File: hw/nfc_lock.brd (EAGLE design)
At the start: 100 x 80 mm, 0 parts

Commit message: CPU + NFC
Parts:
- added IC1: STM8S003F3, stm8:TSSOP20
- added U1: M24SR16-YMN6T/2, m24sr16-ymn6t_2:SOIC127P600X175-8N
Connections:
- new net GND: IC1.7
- new net VCAP: IC1.8
- new net VCC: U1.8
- new net VDD: IC1.9
- new net VSS: U1.4
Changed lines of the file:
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@@
 </autorouter>
 <elements>
+<element name="U1" library="m24sr16-ymn6t_2" package="SOIC127P600X175-8N" value="M24SR16-YMN6T/2" x="20.32" y="17.78">
+<attribute name="PACKAGE" value="SO-8 STMicroelectronics" x="20.32" y="17.78" size="1.778" layer="27" display="off"/>
+<attribute name="PRICE" value="0.81 USD" x="20.32" y="17.78" size="1.778" layer="27" display="off"/>
+<attribute name="MP" value="M24SR16-YMN6T/2" x="20.32" y="17.78" size="1.778" layer="27" display="off"/>
+<attribute name="DESCRIPTION" value=" NFC/RFID Tag and Transponder Chip 13553kHz to 13567kHz 16Kbit 8-Pin SO N Tape and Reel " x="20.32" y="17.78" size="1.778" layer="27" display="off"/>
+<attribute name="AVAILABILITY" value="Good" x="20.32" y="17.78" size="1.778" layer="27" display="off"/>
+<attribute name="MF" value="STMicroelectronics" x="20.32" y="17.78" size="1.778" layer="27" display="off"/>
+</element>
+<element name="IC1" library="stm8" package="TSSOP20" value="STM8S003F3" x="31.75" y="34.29" rot="R270"/>
 </elements>
 <signals>
+<signal name="VCC">
+<contactref element="U1" pad="8"/>
+</signal>
+<signal name="VSS">
+<contactref element="U1" pad="4"/>
+</signal>
+<signal name="VDD">
+<contactref element="IC1" pad="9"/>
+</signal>
+<signal name="VCAP">
+<contactref element="IC1" pad="8"/>
+</signal>
+<signal name="GND">
+<contactref element="IC1" pad="7"/>
+</signal>
 </signals>
 </board>

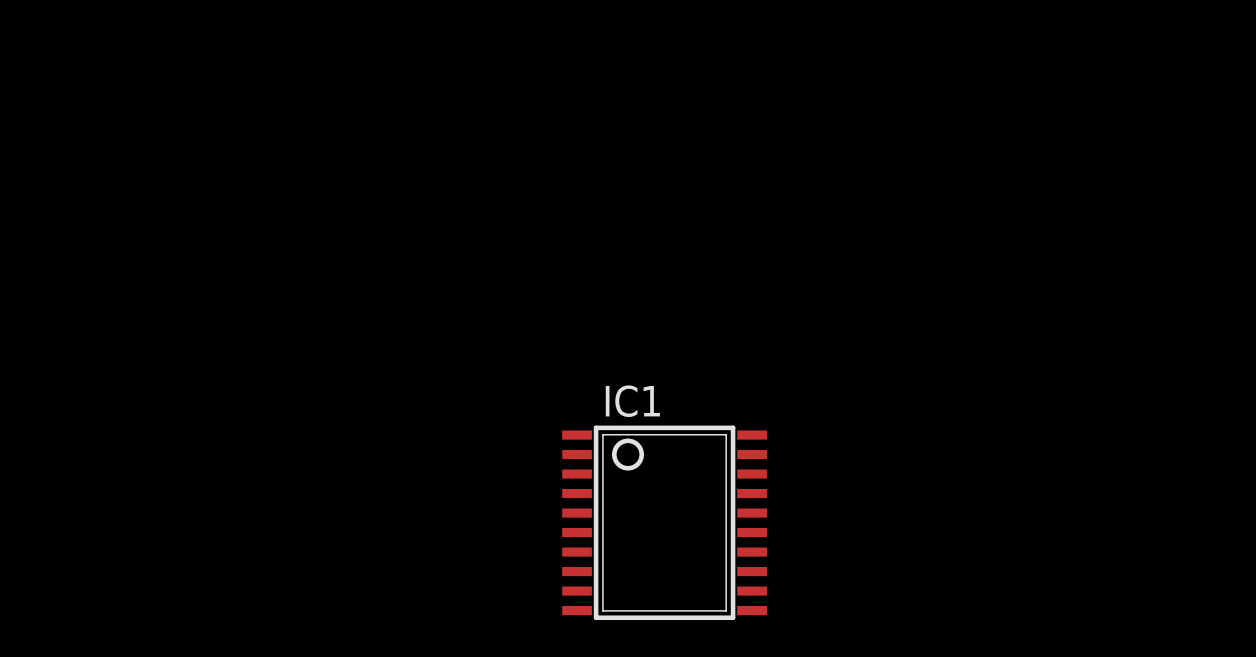
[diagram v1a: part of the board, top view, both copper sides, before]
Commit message: 3.3 voltage regulators + I2C lines
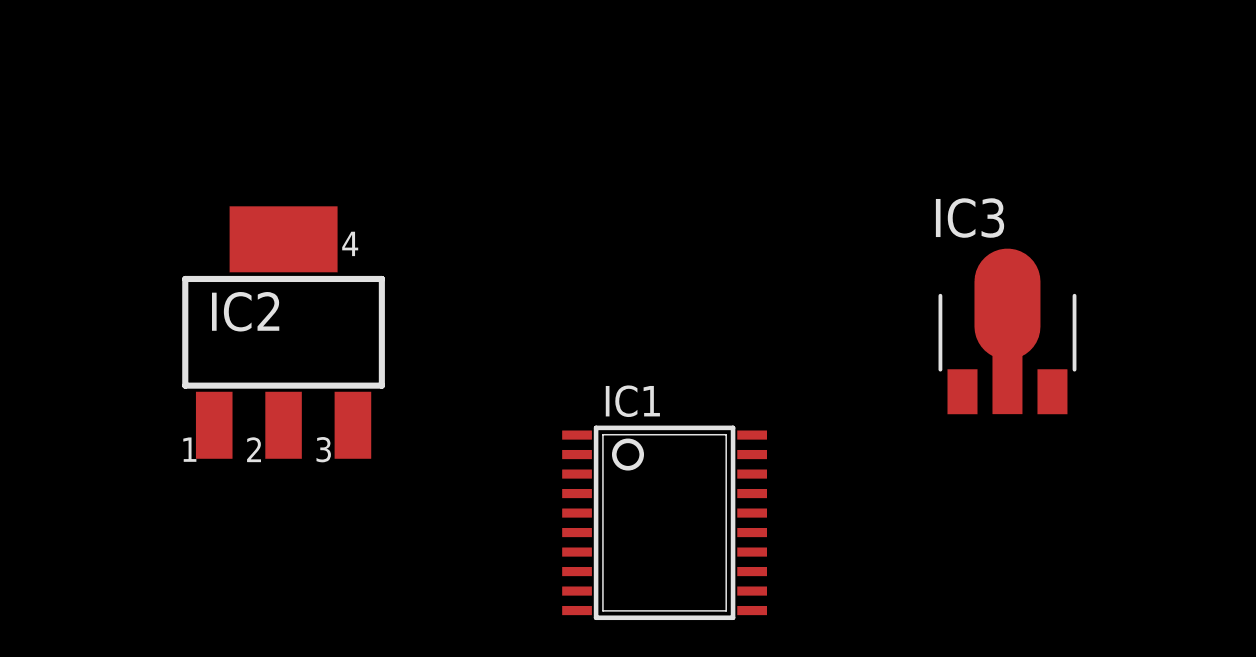
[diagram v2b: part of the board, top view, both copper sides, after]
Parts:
- added IC2: MCP1703DB, linear:SOT223
- added IC3: MCP170312MB, linear:SOT89
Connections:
- new net N$1: IC1.12, U1.6
- new net N$2: IC1.11, U1.5
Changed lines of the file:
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@@
 </element>
 <element name="IC1" library="stm8" package="TSSOP20" value="STM8S003F3" x="31.75" y="34.29" rot="R270"/>
+<element name="IC2" library="linear" package="SOT223" value="MCP1703DB" x="19.05" y="40.64"/>
+<element name="IC3" library="linear" package="SOT89" value="MCP170312MB" x="43.18" y="40.64"/>
 </elements>
 <signals>
@@
 <contactref element="IC1" pad="7"/>
 </signal>
+<signal name="N$1">
+<contactref element="IC1" pad="12"/>
+<contactref element="U1" pad="6"/>
+<wire x1="22.6822" y1="17.145" x2="34.6678" y2="32.015" width="0" layer="19" extent="1-1"/>
+</signal>
+<signal name="N$2">
+<contactref element="IC1" pad="11"/>
+<contactref element="U1" pad="5"/>
+<wire x1="22.6822" y1="15.875" x2="34.6678" y2="31.365" width="0" layer="19" extent="1-1"/>
+</signal>
 </signals>

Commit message: power supply circut
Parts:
- removed IC2: MCP1703DB, linear:SOT223
- added C2: (no value), rcl:153CLV-0405
- added C3: (no value), rcl:C1206
- added D1, D2: GF1, diode:SMA-DO214AC
- moved IC3 7.62 mm to (43.2, 48.3)
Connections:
- new net +5V: D1.A
- new net +5V/1: C3.1, IC3.3
- new net 0V: C2.-, C3.2, IC3.1
- new net N$3: D1.K, D2.A
- new net N$4: C2.+, D2.K, IC3.2@1
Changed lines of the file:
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@@
 <layer number="97" name="Info" color="7" fill="1" visible="no" active="no"/>
 <layer number="98" name="Guide" color="6" fill="1" visible="no" active="no"/>
+<layer number="99" name="SpiceOrder" color="5" fill="1" visible="no" active="no"/>
 </layers>
 <board>
@@
 </element>
 <element name="IC1" library="stm8" package="TSSOP20" value="STM8S003F3" x="31.75" y="34.29" rot="R270"/>
-<element name="IC2" library="linear" package="SOT223" value="MCP1703DB" x="19.05" y="40.64"/>
-<element name="IC3" library="linear" package="SOT89" value="MCP170312MB" x="43.18" y="40.64"/>
+<element name="IC3" library="linear" package="SOT89" value="MCP170312MB" x="43.18" y="48.26"/>
+<element name="C2" library="rcl" package="153CLV-0405" value="" x="36.83" y="48.26" rot="R90"/>
+<element name="C3" library="rcl" package="C1206" value="" x="43.18" y="41.91" rot="R180"/>
+<element name="D1" library="diode" package="SMA-DO214AC" value="GF1" x="31.75" y="54.61"/>
+<element name="D2" library="diode" package="SMA-DO214AC" value="GF1" x="41.91" y="54.61"/>
 </elements>
 <signals>
@@
 <wire x1="22.6822" y1="15.875" x2="34.6678" y2="31.365" width="0" layer="19" extent="1-1"/>
 </signal>
+<signal name="0V">
+<contactref element="IC3" pad="1"/>
+<contactref element="C3" pad="2"/>
+<contactref element="C2" pad="-"/>
+<wire x1="41.681" y1="46.279" x2="41.78" y2="41.91" width="0" layer="19" extent="1-1"/>
+<wire x1="36.83" y1="46.46" x2="41.681" y2="46.279" width="0" layer="19" extent="1-1"/>
+</signal>
+<signal name="+5V/1">
+<contactref element="IC3" pad="3"/>
+<contactref element="C3" pad="1"/>
+<wire x1="44.679" y1="46.279" x2="44.58" y2="41.91" width="0" layer="19" extent="1-1"/>
+</signal>
+<signal name="+5V">
+<contactref element="D1" pad="A"/>
+</signal>
+<signal name="N$3">
+<contactref element="D1" pad="K"/>
+<contactref element="D2" pad="A"/>
+<wire x1="39.86" y1="54.61" x2="33.8" y2="54.61" width="0" layer="19" extent="1-1"/>
+</signal>
+<signal name="N$4">
+<contactref element="IC3" pad="2@1"/>
+<contactref element="D2" pad="K"/>
+<contactref element="C2" pad="+"/>
+<wire x1="36.83" y1="50.06" x2="43.18" y2="49.2" width="0" layer="19" extent="1-1"/>
+<wire x1="43.96" y1="54.61" x2="43.18" y2="49.2" width="0" layer="19" extent="1-1"/>
+</signal>
 </signals>

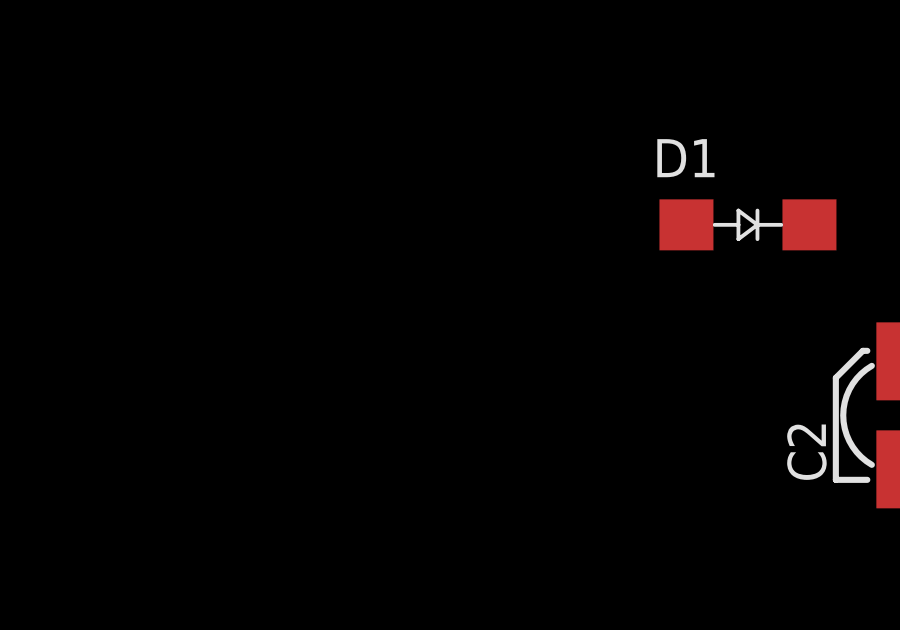
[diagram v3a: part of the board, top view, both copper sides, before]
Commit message: power supply pads added
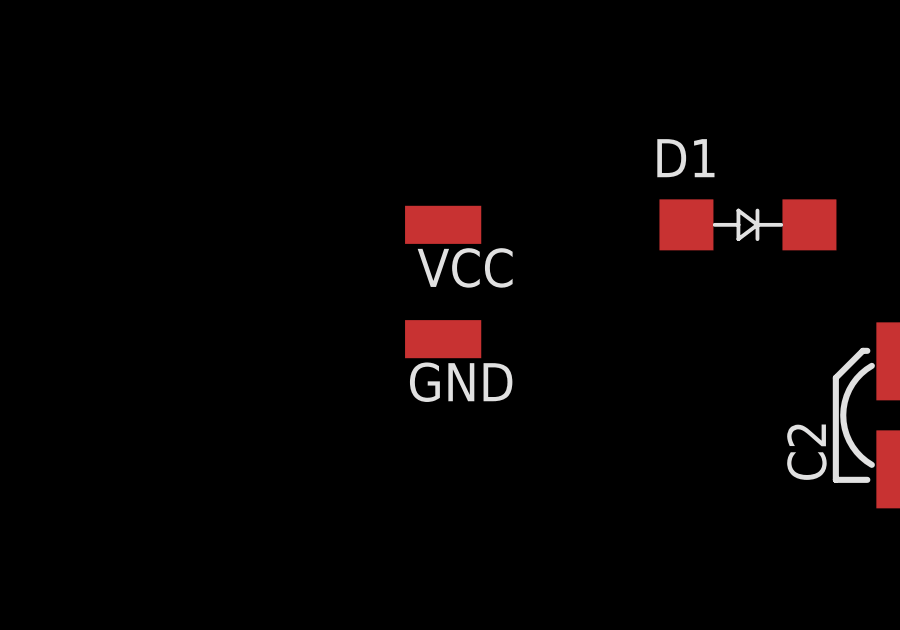
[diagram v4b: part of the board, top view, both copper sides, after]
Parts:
- added GND, VCC: (no value), wirepad:SMD1,27-2,54
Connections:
- net +5V: now also VCC.1
- net 0V: now also GND.1
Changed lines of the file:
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@@
 <element name="D1" library="diode" package="SMA-DO214AC" value="GF1" x="31.75" y="54.61"/>
 <element name="D2" library="diode" package="SMA-DO214AC" value="GF1" x="41.91" y="54.61"/>
+<element name="VCC" library="wirepad" package="SMD1,27-2,54" value="" x="21.59" y="54.61" rot="R90"/>
+<element name="GND" library="wirepad" package="SMD1,27-2,54" value="" x="21.59" y="50.8" rot="R90"/>
 </elements>
 <signals>
@@
 <contactref element="C3" pad="2"/>
 <contactref element="C2" pad="-"/>
-<wire x1="41.681" y1="46.279" x2="41.78" y2="41.91" width="0" layer="19" extent="1-1"/>
+<contactref element="GND" pad="1"/>
+<wire x1="41.78" y1="41.91" x2="41.681" y2="46.279" width="0" layer="19" extent="1-1"/>
 <wire x1="36.83" y1="46.46" x2="41.681" y2="46.279" width="0" layer="19" extent="1-1"/>
+<wire x1="21.59" y1="50.8" x2="41.78" y2="41.91" width="0" layer="19" extent="1-1"/>
 </signal>
 <signal name="+5V/1">
@@
 <signal name="+5V">
 <contactref element="D1" pad="A"/>
+<contactref element="VCC" pad="1"/>
+<wire x1="21.59" y1="54.61" x2="29.7" y2="54.61" width="0" layer="19" extent="1-1"/>
 </signal>
 <signal name="N$3">

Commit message: USB powersupply
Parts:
- removed GND, VCC: (no value), wirepad:SMD1,27-2,54
- added X1: MINI-USB-32005-301, con-cypressindustries:32005-301
- moved U1 14.5 mm to (31.8, 26.7)
- moved D1 2.54 mm to (31.8, 52.1), turned to 90 degrees
- moved IC1 1.27 mm to (31.8, 35.6)
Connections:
- removed net GND: IC1.7
- removed net VCC: U1.8
- removed net VDD: IC1.9
- removed net VSS: U1.4
- net +5V: now also X1.1; no longer VCC.1
- net +5V/1: now also IC1.9, U1.8
- net 0V: now also IC1.7, U1.4, X1.5; no longer GND.1
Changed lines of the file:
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@@
 </autorouter>
 <elements>
-<element name="U1" library="m24sr16-ymn6t_2" package="SOIC127P600X175-8N" value="M24SR16-YMN6T/2" x="20.32" y="17.78">
-<attribute name="PACKAGE" value="SO-8 STMicroelectronics" x="20.32" y="17.78" size="1.778" layer="27" display="off"/>
-<attribute name="PRICE" value="0.81 USD" x="20.32" y="17.78" size="1.778" layer="27" display="off"/>
-<attribute name="MP" value="M24SR16-YMN6T/2" x="20.32" y="17.78" size="1.778" layer="27" display="off"/>
-<attribute name="DESCRIPTION" value=" NFC/RFID Tag and Transponder Chip 13553kHz to 13567kHz 16Kbit 8-Pin SO N Tape and Reel " x="20.32" y="17.78" size="1.778" layer="27" display="off"/>
-<attribute name="AVAILABILITY" value="Good" x="20.32" y="17.78" size="1.778" layer="27" display="off"/>
-<attribute name="MF" value="STMicroelectronics" x="20.32" y="17.78" size="1.778" layer="27" display="off"/>
+<element name="U1" library="m24sr16-ymn6t_2" package="SOIC127P600X175-8N" value="M24SR16-YMN6T/2" x="31.75" y="26.67">
+<attribute name="PACKAGE" value="SO-8 STMicroelectronics" x="31.75" y="26.67" size="1.778" layer="27" display="off"/>
+<attribute name="PRICE" value="0.81 USD" x="31.75" y="26.67" size="1.778" layer="27" display="off"/>
+<attribute name="MP" value="M24SR16-YMN6T/2" x="31.75" y="26.67" size="1.778" layer="27" display="off"/>
+<attribute name="DESCRIPTION" value=" NFC/RFID Tag and Transponder Chip 13553kHz to 13567kHz 16Kbit 8-Pin SO N Tape and Reel " x="31.75" y="26.67" size="1.778" layer="27" display="off"/>
+<attribute name="AVAILABILITY" value="Good" x="31.75" y="26.67" size="1.778" layer="27" display="off"/>
+<attribute name="MF" value="STMicroelectronics" x="31.75" y="26.67" size="1.778" layer="27" display="off"/>
 </element>
-<element name="IC1" library="stm8" package="TSSOP20" value="STM8S003F3" x="31.75" y="34.29" rot="R270"/>
+<element name="IC1" library="stm8" package="TSSOP20" value="STM8S003F3" x="31.75" y="35.56" rot="R270"/>
 <element name="IC3" library="linear" package="SOT89" value="MCP170312MB" x="43.18" y="48.26"/>
 <element name="C2" library="rcl" package="153CLV-0405" value="" x="36.83" y="48.26" rot="R90"/>
 <element name="C3" library="rcl" package="C1206" value="" x="43.18" y="41.91" rot="R180"/>
-<element name="D1" library="diode" package="SMA-DO214AC" value="GF1" x="31.75" y="54.61"/>
+<element name="D1" library="diode" package="SMA-DO214AC" value="GF1" x="31.75" y="52.07" rot="R90"/>
 <element name="D2" library="diode" package="SMA-DO214AC" value="GF1" x="41.91" y="54.61"/>
-<element name="VCC" library="wirepad" package="SMD1,27-2,54" value="" x="21.59" y="54.61" rot="R90"/>
-<element name="GND" library="wirepad" package="SMD1,27-2,54" value="" x="21.59" y="50.8" rot="R90"/>
+<element name="X1" library="con-cypressindustries" package="32005-301" value="MINI-USB-32005-301" x="22.86" y="50.8">
+<attribute name="OC_FARNELL" value="unknown" x="22.86" y="50.8" size="1.778" layer="27" display="off"/>
+<attribute name="MPN" value="" x="22.86" y="50.8" size="1.778" layer="27" display="off"/>
+<attribute name="MF" value="" x="22.86" y="50.8" size="1.778" layer="27" display="off"/>
+<attribute name="OC_NEWARK" value="unknown" x="22.86" y="50.8" size="1.778" layer="27" display="off"/>
+</element>
 </elements>
 <signals>
-<signal name="VCC">
-<contactref element="U1" pad="8"/>
-</signal>
-<signal name="VSS">
-<contactref element="U1" pad="4"/>
-</signal>
-<signal name="VDD">
-<contactref element="IC1" pad="9"/>
-</signal>
 <signal name="VCAP">
 <contactref element="IC1" pad="8"/>
-</signal>
-<signal name="GND">
-<contactref element="IC1" pad="7"/>
 </signal>
 <signal name="N$1">
 <contactref element="IC1" pad="12"/>
 <contactref element="U1" pad="6"/>
-<wire x1="22.6822" y1="17.145" x2="34.6678" y2="32.015" width="0" layer="19" extent="1-1"/>
+<wire x1="34.1122" y1="26.035" x2="34.6678" y2="33.285" width="0" layer="19" extent="1-1"/>
 </signal>
 <signal name="N$2">
 <contactref element="IC1" pad="11"/>
 <contactref element="U1" pad="5"/>
-<wire x1="22.6822" y1="15.875" x2="34.6678" y2="31.365" width="0" layer="19" extent="1-1"/>
+<wire x1="34.1122" y1="24.765" x2="34.6678" y2="32.635" width="0" layer="19" extent="1-1"/>
 </signal>
 <signal name="0V">
@@
 <contactref element="C3" pad="2"/>
 <contactref element="C2" pad="-"/>
-<contactref element="GND" pad="1"/>
+<contactref element="X1" pad="5"/>
+<contactref element="IC1" pad="7"/>
+<contactref element="U1" pad="4"/>
 <wire x1="41.78" y1="41.91" x2="41.681" y2="46.279" width="0" layer="19" extent="1-1"/>
 <wire x1="36.83" y1="46.46" x2="41.681" y2="46.279" width="0" layer="19" extent="1-1"/>
-<wire x1="21.59" y1="50.8" x2="41.78" y2="41.91" width="0" layer="19" extent="1-1"/>
+<wire x1="25.86" y1="49.2" x2="36.83" y2="46.46" width="0" layer="19" extent="1-1"/>
+<wire x1="28.8322" y1="34.585" x2="36.83" y2="46.46" width="0" layer="19" extent="1-1"/>
+<wire x1="29.3878" y1="24.765" x2="28.8322" y2="34.585" width="0" layer="19" extent="1-1"/>
 </signal>
 <signal name="+5V/1">
 <contactref element="IC3" pad="3"/>
 <contactref element="C3" pad="1"/>
-<wire x1="44.679" y1="46.279" x2="44.58" y2="41.91" width="0" layer="19" extent="1-1"/>
+<contactref element="IC1" pad="9"/>
+<contactref element="U1" pad="8"/>
+<wire x1="44.58" y1="41.91" x2="44.679" y2="46.279" width="0" layer="19" extent="1-1"/>
+<wire x1="28.8322" y1="33.285" x2="44.58" y2="41.91" width="0" layer="19" extent="1-1"/>
+<wire x1="34.1122" y1="28.575" x2="28.8322" y2="33.285" width="0" layer="19" extent="1-1"/>
 </signal>
 <signal name="+5V">
 <contactref element="D1" pad="A"/>
-<contactref element="VCC" pad="1"/>
-<wire x1="21.59" y1="54.61" x2="29.7" y2="54.61" width="0" layer="19" extent="1-1"/>
+<contactref element="X1" pad="1"/>
+<wire x1="25.86" y1="52.4" x2="31.75" y2="50.02" width="0" layer="19" extent="1-1"/>
 </signal>
 <signal name="N$3">
 <contactref element="D1" pad="K"/>
 <contactref element="D2" pad="A"/>
-<wire x1="39.86" y1="54.61" x2="33.8" y2="54.61" width="0" layer="19" extent="1-1"/>
+<wire x1="39.86" y1="54.61" x2="31.75" y2="54.12" width="0" layer="19" extent="1-1"/>
 </signal>
 <signal name="N$4">
